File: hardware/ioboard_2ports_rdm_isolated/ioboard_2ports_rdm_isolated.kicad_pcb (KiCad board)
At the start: 2 copper layers, 106 x 55 mm, 30 parts, among them J1 Conn_02x06_Odd_Even, J12 Conn_01x03, J2 XLR3, J3 XLR3, J6 Conn_01x03, J8 XLR3, J9 XLR3, U1 M24C02-WMN, U2 CRE1S0505DC, U4 ADM2483xRW, U6 ADM2483xRW

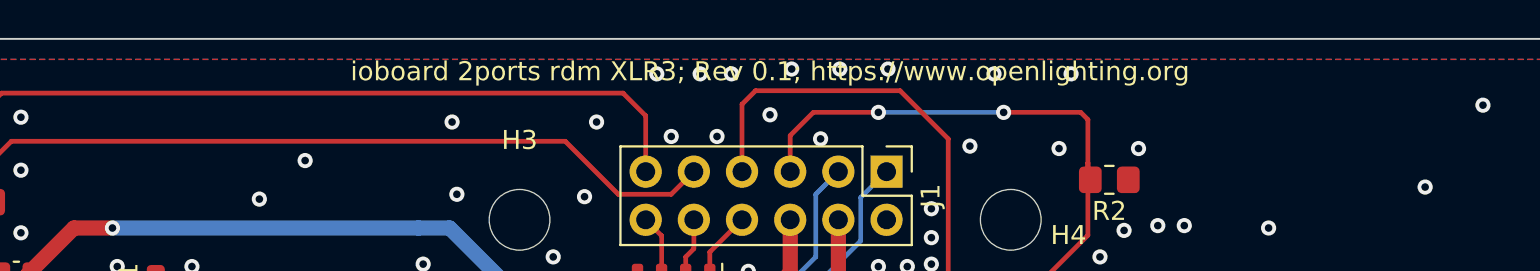
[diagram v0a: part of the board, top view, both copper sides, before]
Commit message: Unify board naming and bump all to rev 0.2
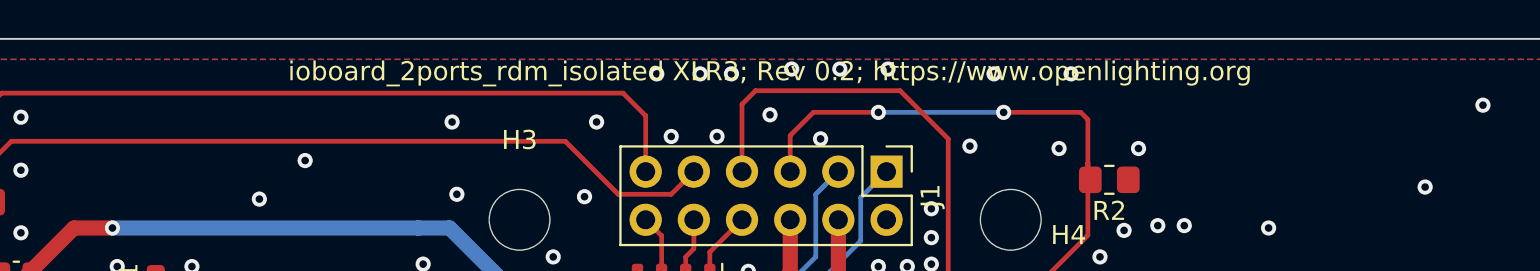
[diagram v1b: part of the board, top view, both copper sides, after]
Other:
- board text added: "ioboard_2ports_rdm_isolated XLR3; Rev 0.2; https://www.openlighting.org"
- board text removed: "ioboard 2ports rdm XLR3; Rev 0.1; https://www.openlighting.org"
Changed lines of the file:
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@@
   (page A4)
   (title_block
-    (title "rp2040_dongle ioboard 2slots rdm")
-    (date 2021-03-21)
-    (rev 0.1)
+    (title rp2040_dongle_ioboard_2ports_rdm_isolated)
+    (date 2021-03-28)
+    (rev 0.2)
     (company https://www.openlighting.org)
   )
@@
     (arrow2b (pts (xy 21.082 20) (xy 21.668421 21.126504)))
   )
-  (gr_text "ioboard 2ports rdm XLR3; Rev 0.1; https://www.openlighting.org" (at 78.105 21.717) (layer F.SilkS)
+  (gr_text "ioboard_2ports_rdm_isolated XLR3; Rev 0.2; https://www.openlighting.org" (at 78.105 21.717) (layer F.SilkS)
     (effects (font (size 1 1) (thickness 0.15)))
   )
@@
   (via (at 77.978 37.338) (size 0.8) (drill 0.4) (layers F.Cu B.Cu) (net 9))
   (via (at 76.962 32.258) (size 0.8) (drill 0.4) (layers F.Cu B.Cu) (net 9))
+  (segment (start 84.25 27) (end 82.885001 28.364999) (width 0.25) (layer B.Cu) (net 10))
+  (segment (start 82.885001 30.652999) (end 76.454 37.084) (width 0.25) (layer B.Cu) (net 10))
+  (segment (start 82.885001 28.364999) (end 82.885001 30.652999) (width 0.25) (layer B.Cu) (net 10))
+  (via (at 69.85 37.084) (size 0.8) (drill 0.4) (layers F.Cu B.Cu) (net 10))
+  (segment (start 70.547 37.781) (end 71.12 37.781) (width 0.25) (layer F.Cu) (net 10))
+  (segment (start 70.547 37.781) (end 69.85 37.084) (width 0.25) (layer F.Cu) (net 10))
+  (segment (start 69.85 37.084) (end 76.454 37.084) (width 0.25) (layer B.Cu) (net 10))
+  (segment (start 36.474999 65.224999) (end 36.474999 60.807001) (width 0.25) (layer F.Cu) (net 11))
+  (segment (start 38.25 67) (end 36.474999 65.224999) (width 0.25) (layer F.Cu) (net 11))
+  (segment (start 38.25 59.032) (end 38.25 56.162) (width 0.25) (layer F.Cu) (net 11))
+  (segment (start 36.474999 60.807001) (end 38.25 59.032) (width 0.25) (layer F.Cu) (net 11))
+  (segment (start 38.354 56.058) (end 38.25 56.162) (width 0.25) (layer F.Cu) (net 11))
+  (segment (start 38.354 51.054) (end 38.354 56.058) (width 0.25) (layer F.Cu) (net 11))
+  (segment (start 33.909 44.782) (end 33.909 46.609) (width 0.25) (layer F.Cu) (net 11))
+  (segment (start 33.6315 46.8865) (end 33.6315 47.752) (width 0.25) (layer F.Cu) (net 11))
+  (segment (start 33.909 46.609) (end 33.6315 46.8865) (width 0.25) (layer F.Cu) (net 11))
+  (via (at 32.004 47.752) (size 0.8) (drill 0.4) (layers F.Cu B.Cu) (net 11))
+  (segment (start 33.6315 47.752) (end 32.004 47.752) (width 0.25) (layer F.Cu) (net 11))
+  (via (at 38.354 47.752) (size 0.8) (drill 0.4) (layers F.Cu B.Cu) (net 11))
+  (segment (start 32.004 47.752) (end 38.354 47.752) (width 0.25) (layer B.Cu) (net 11))
+  (segment (start 38.354 47.752) (end 38.354 51.054) (width 0.25) (layer F.Cu) (net 11))
+  (segment (start 44.958 51.054) (end 44.958 52.832) (width 0.25) (layer F.Cu) (net 11))
+  (segment (start 41.628 56.162) (end 38.25 56.162) (width 0.25) (layer F.Cu) (net 11))
+  (segment (start 44.958 52.832) (end 41.628 56.162) (width 0.25) (layer F.Cu) (net 11))
   (via (at 48.006 43.942) (size 0.8) (drill 0.4) (layers F.Cu B.Cu) (net 12))
   (via (at 48.006 41.91) (size 0.8) (drill 0.4) (layers F.Cu B.Cu) (net 12))
@@
   (via (at 119.888 54.229) (size 0.8) (drill 0.4) (layers F.Cu B.Cu) (net 12))
   (via (at 115.697 43.18) (size 0.8) (drill 0.4) (layers F.Cu B.Cu) (net 12))
-  (segment (start 84.25 27) (end 82.885001 28.364999) (width 0.25) (layer B.Cu) (net 10))
-  (segment (start 82.885001 30.652999) (end 76.454 37.084) (width 0.25) (layer B.Cu) (net 10))
-  (segment (start 82.885001 28.364999) (end 82.885001 30.652999) (width 0.25) (layer B.Cu) (net 10))
-  (via (at 69.85 37.084) (size 0.8) (drill 0.4) (layers F.Cu B.Cu) (net 10))
-  (segment (start 70.547 37.781) (end 71.12 37.781) (width 0.25) (layer F.Cu) (net 10))
-  (segment (start 70.547 37.781) (end 69.85 37.084) (width 0.25) (layer F.Cu) (net 10))
-  (segment (start 69.85 37.084) (end 76.454 37.084) (width 0.25) (layer B.Cu) (net 10))
-  (segment (start 36.474999 65.224999) (end 36.474999 60.807001) (width 0.25) (layer F.Cu) (net 11))
-  (segment (start 38.25 67) (end 36.474999 65.224999) (width 0.25) (layer F.Cu) (net 11))
-  (segment (start 38.25 59.032) (end 38.25 56.162) (width 0.25) (layer F.Cu) (net 11))
-  (segment (start 36.474999 60.807001) (end 38.25 59.032) (width 0.25) (layer F.Cu) (net 11))
-  (segment (start 38.354 56.058) (end 38.25 56.162) (width 0.25) (layer F.Cu) (net 11))
-  (segment (start 38.354 51.054) (end 38.354 56.058) (width 0.25) (layer F.Cu) (net 11))
-  (segment (start 33.909 44.782) (end 33.909 46.609) (width 0.25) (layer F.Cu) (net 11))
-  (segment (start 33.6315 46.8865) (end 33.6315 47.752) (width 0.25) (layer F.Cu) (net 11))
-  (segment (start 33.909 46.609) (end 33.6315 46.8865) (width 0.25) (layer F.Cu) (net 11))
-  (via (at 32.004 47.752) (size 0.8) (drill 0.4) (layers F.Cu B.Cu) (net 11))
-  (segment (start 33.6315 47.752) (end 32.004 47.752) (width 0.25) (layer F.Cu) (net 11))
-  (via (at 38.354 47.752) (size 0.8) (drill 0.4) (layers F.Cu B.Cu) (net 11))
-  (segment (start 32.004 47.752) (end 38.354 47.752) (width 0.25) (layer B.Cu) (net 11))
-  (segment (start 38.354 47.752) (end 38.354 51.054) (width 0.25) (layer F.Cu) (net 11))
-  (segment (start 44.958 51.054) (end 44.958 52.832) (width 0.25) (layer F.Cu) (net 11))
-  (segment (start 41.628 56.162) (end 38.25 56.162) (width 0.25) (layer F.Cu) (net 11))
-  (segment (start 44.958 52.832) (end 41.628 56.162) (width 0.25) (layer F.Cu) (net 11))
   (via (at 91.948 42.418) (size 0.8) (drill 0.4) (layers F.Cu B.Cu) (net 12))
   (via (at 85.598 42.418) (size 0.8) (drill 0.4) (layers F.Cu B.Cu) (net 12))

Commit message: Hardware: Make the reference path to the library relative and save the files with the new kicad version
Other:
- net class Default removed

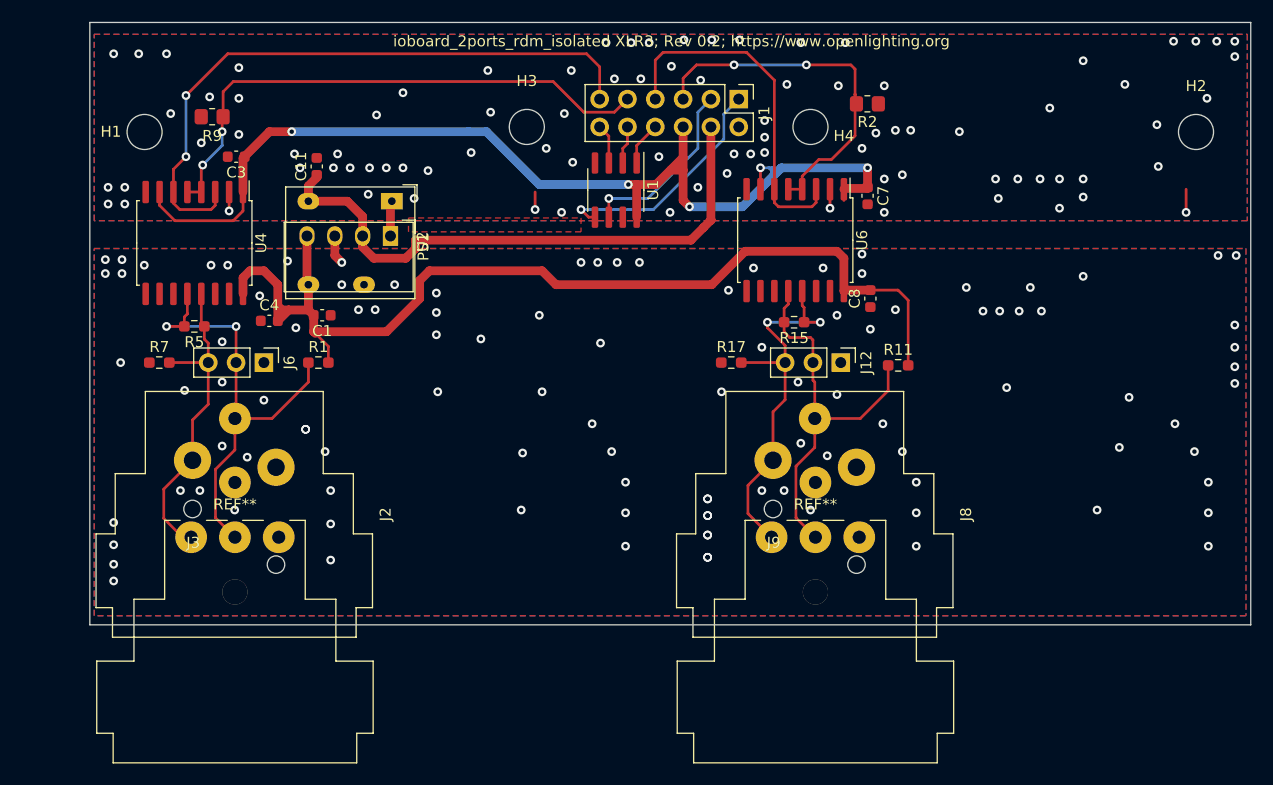
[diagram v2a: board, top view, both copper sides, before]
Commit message: Fix gitignore Move NC3FD-H.pretty footprint library to a common location and update references Rework ioboard_2ports_rdm_isolated
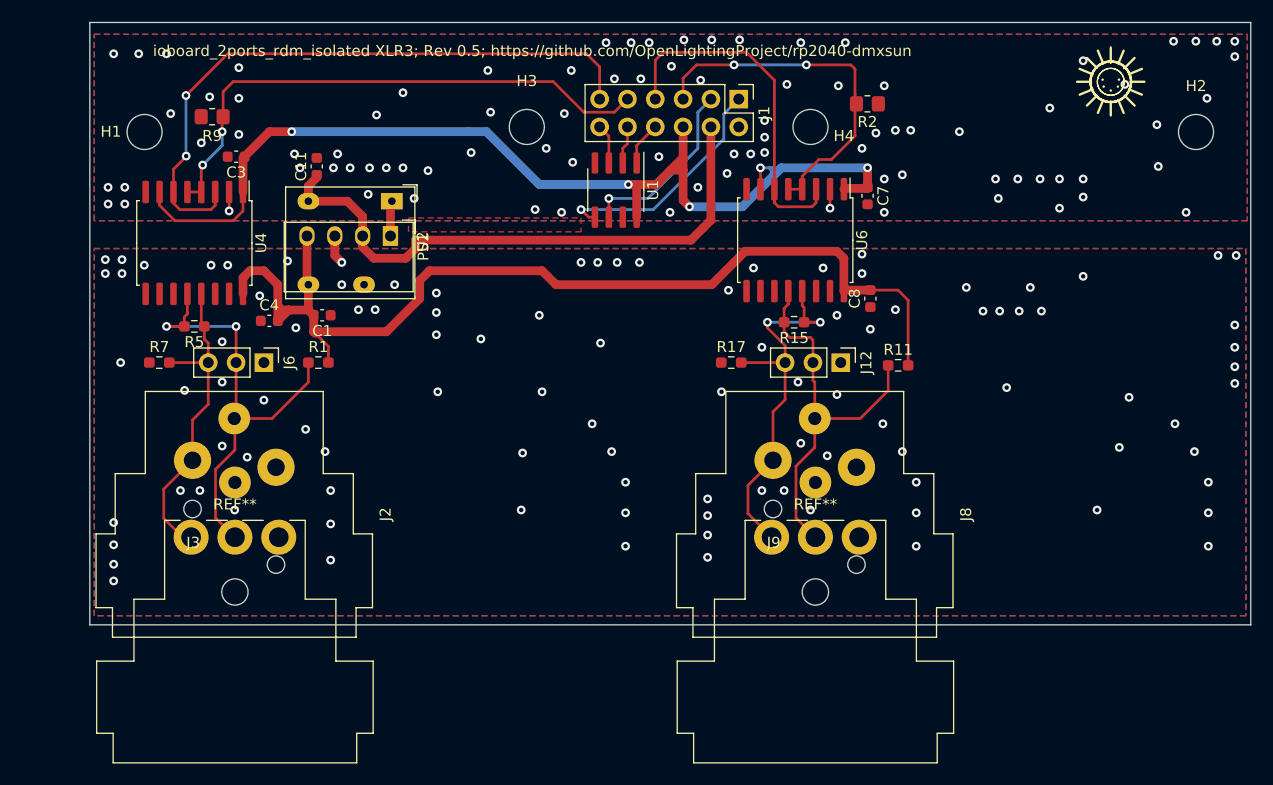
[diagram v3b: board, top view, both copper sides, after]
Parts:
- U1: value M24C02-WMN -> M24C64-RMN6TP
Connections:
- U4 pad 10: (no net) -> unconnected-(U4-Pad10)
- U4 pad 11: (no net) -> unconnected-(U4-Pad11)
- U4 pad 14: (no net) -> unconnected-(U4-Pad14)
- U6 pad 10: (no net) -> unconnected-(U6-Pad10)
- U6 pad 11: (no net) -> unconnected-(U6-Pad11)
- U6 pad 14: (no net) -> unconnected-(U6-Pad14)
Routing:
- net GND: track 10.0 -> 6.69 mm
- net +3V3: track 99.0 -> 97.9 mm
- net /GP3: track 34.4 -> 33.4 mm
- net /GND_1+2: vias 106 -> 101
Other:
- board text added: "ioboard_2ports_rdm_isolated XLR3; Rev 0.5; https://github.com/OpenLightingProject/rp2040-dmxsun"
- board text removed: "ioboard_2ports_rdm_isolated XLR3; Rev 0.2; https://www.openlighting.org"

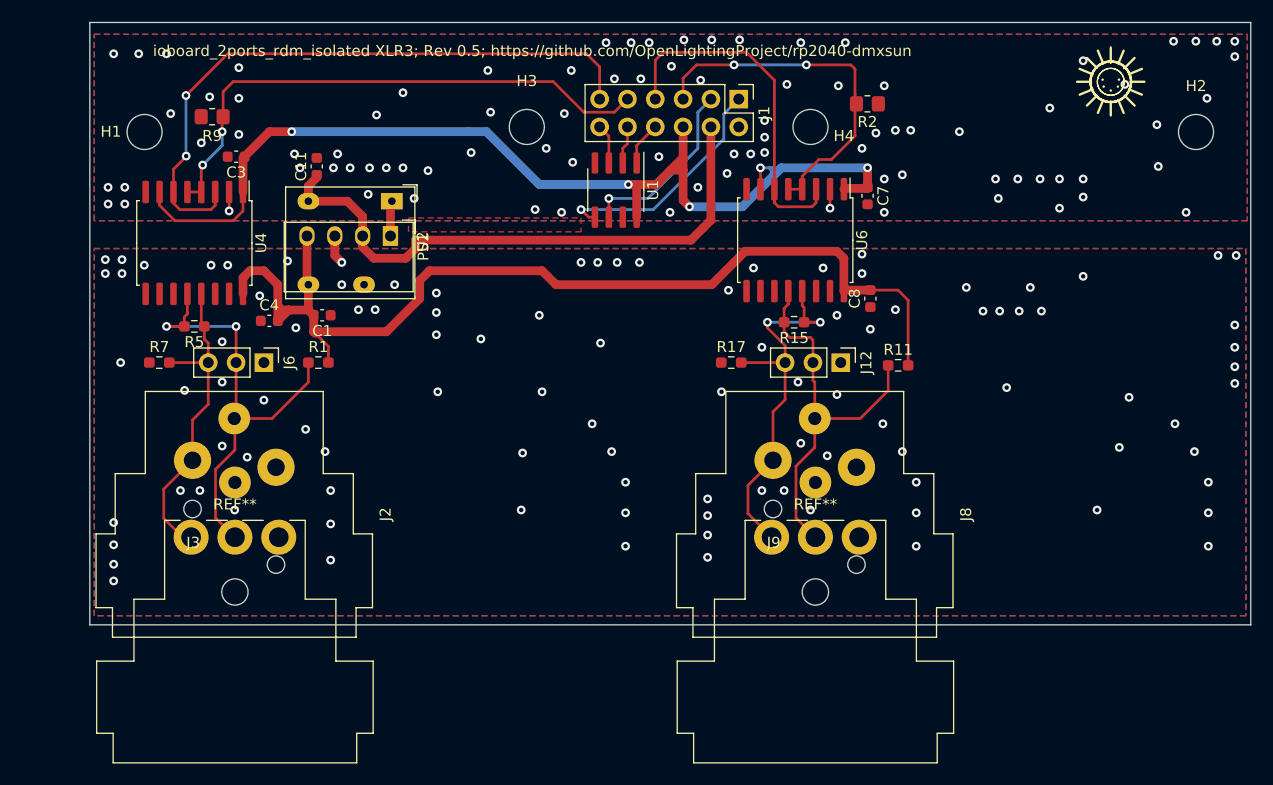
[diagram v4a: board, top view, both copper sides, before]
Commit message: Add an RJ45 connector to ioboard_2ports_rdm_isolated
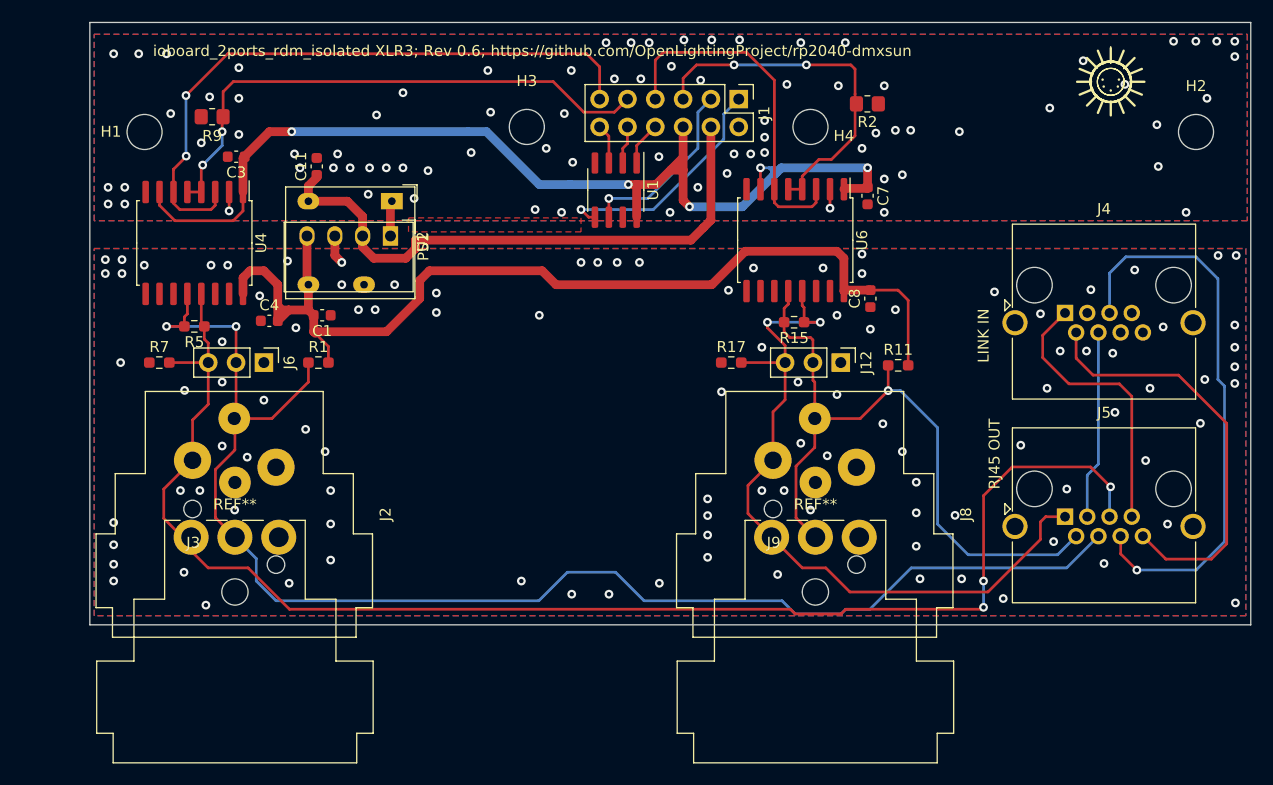
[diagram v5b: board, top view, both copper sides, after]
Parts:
- added J4: 8P8C, Connector_RJ:RJ45_Amphenol_RJHSE5380, F.Cu at (114.0, 46.5)
- added J5: 8P8C, Connector_RJ:RJ45_Amphenol_RJHSE5380, F.Cu at (114.0, 65.1)
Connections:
- net Net-(J12-Pad2) renamed /RJ45_OUT_4
- net Net-(J12-Pad3) renamed /RJ45_OUT_3
- net Net-(J2-Pad2) renamed /RJ45_OUT_2
- net Net-(J2-Pad3) renamed /RJ45_OUT_1
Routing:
- net /RJ45_OUT_2: track 29.2 -> 131.8 mm, vias 0 -> 3
- net /RJ45_OUT_1: track 41.7 -> 129.7 mm
- net /RJ45_LINK_2: track 0.00 -> 52.0 mm, vias 0 -> 1
- net /RJ45_LINK_4: track 0.00 -> 38.7 mm
- net /RJ45_OUT_3: track 35.8 -> 68.5 mm
- net /RJ45_OUT_4: track 36.4 -> 65.6 mm, vias 0 -> 1
- net /RJ45_LINK_3: track 0.00 -> 25.5 mm
- net /RJ45_LINK_1: track 0.00 -> 17.2 mm
- net GND: vias 89 -> 81
- net /GND_1+2: vias 101 -> 105
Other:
- board text added: "LINK IN"
- board text added: "RJ45 OUT"
- board text added: "ioboard_2ports_rdm_isolated XLR3; Rev 0.6; https://github.com/OpenLightingProject/rp2040-dmxsun"
- board text removed: "ioboard_2ports_rdm_isolated XLR3; Rev 0.5; https://github.com/OpenLightingProject/rp2040-dmxsun"

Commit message: Replace Amphenol's RJ45 by the one by Sparkfun/4UCON
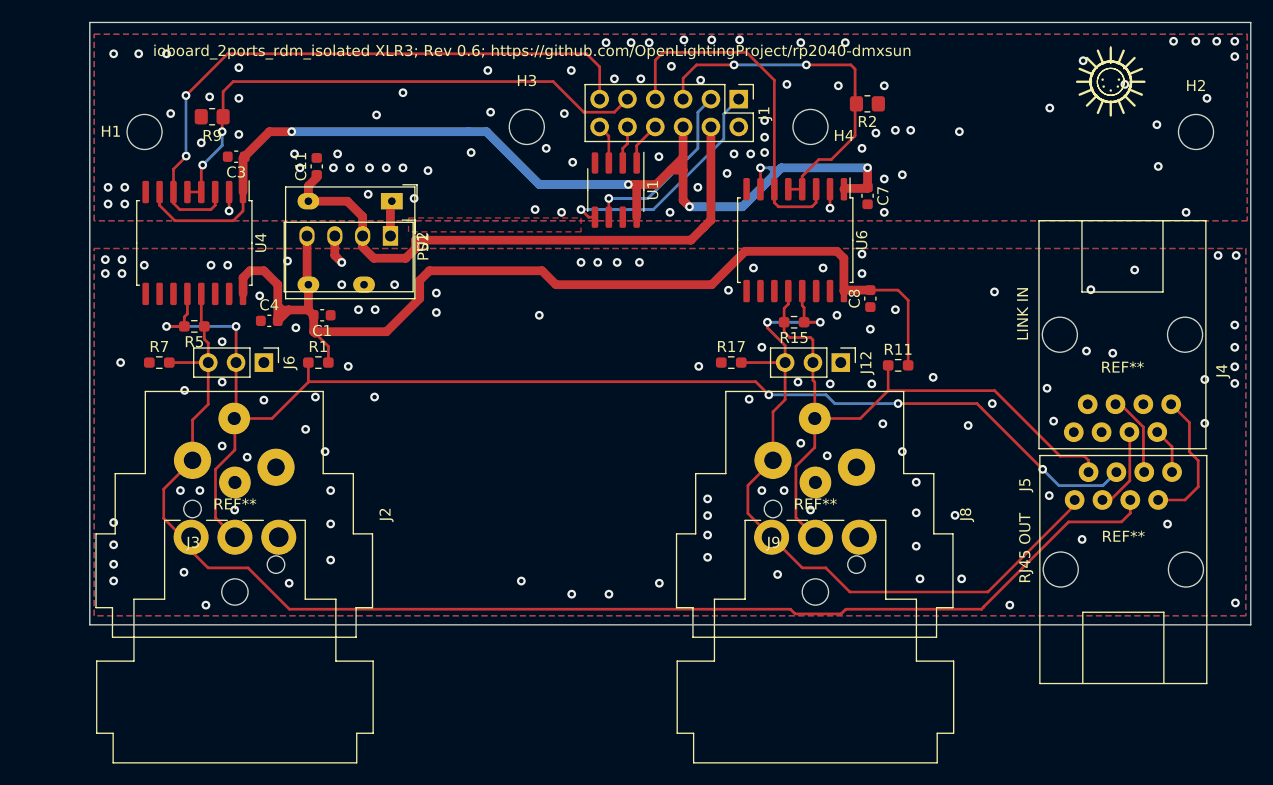
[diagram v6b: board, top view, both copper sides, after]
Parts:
- J4, J5: footprint Connector_RJ:RJ45_Amphenol_RJHSE5380 -> RJ45_Sparkfun:RJ45_Sparkfun
- moved J5 7.19 mm to (119.4, 70.0)
- moved J4 5.61 mm to (119.3, 48.5), turned to 180 degrees
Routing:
- net /RJ45_LINK_2: track 52.0 -> 7.55 mm, vias 1 -> 0
- net /RJ45_LINK_4: track 38.7 -> 4.21 mm
- net /RJ45_LINK_3: track 25.5 -> 12.7 mm
- net /RJ45_OUT_1: track 129.7 -> 119.9 mm, vias 2 -> 5
- net /RJ45_LINK_1: track 17.2 -> 7.68 mm
- net /RJ45_OUT_2: track 131.8 -> 123.6 mm, vias 3 -> 0
- net /RJ45_OUT_4: track 65.6 -> 58.4 mm, vias 1 -> 0
- net /RJ45_OUT_3: track 68.5 -> 69.3 mm
- net /GND_1+2: vias 105 -> 106
